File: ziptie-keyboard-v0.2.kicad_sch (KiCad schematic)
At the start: 149 parts, among them J1 Conn_01x01_Socket, J2 Conn_01x01_Socket, SW1 RotaryEncoder, U1 nice_nano

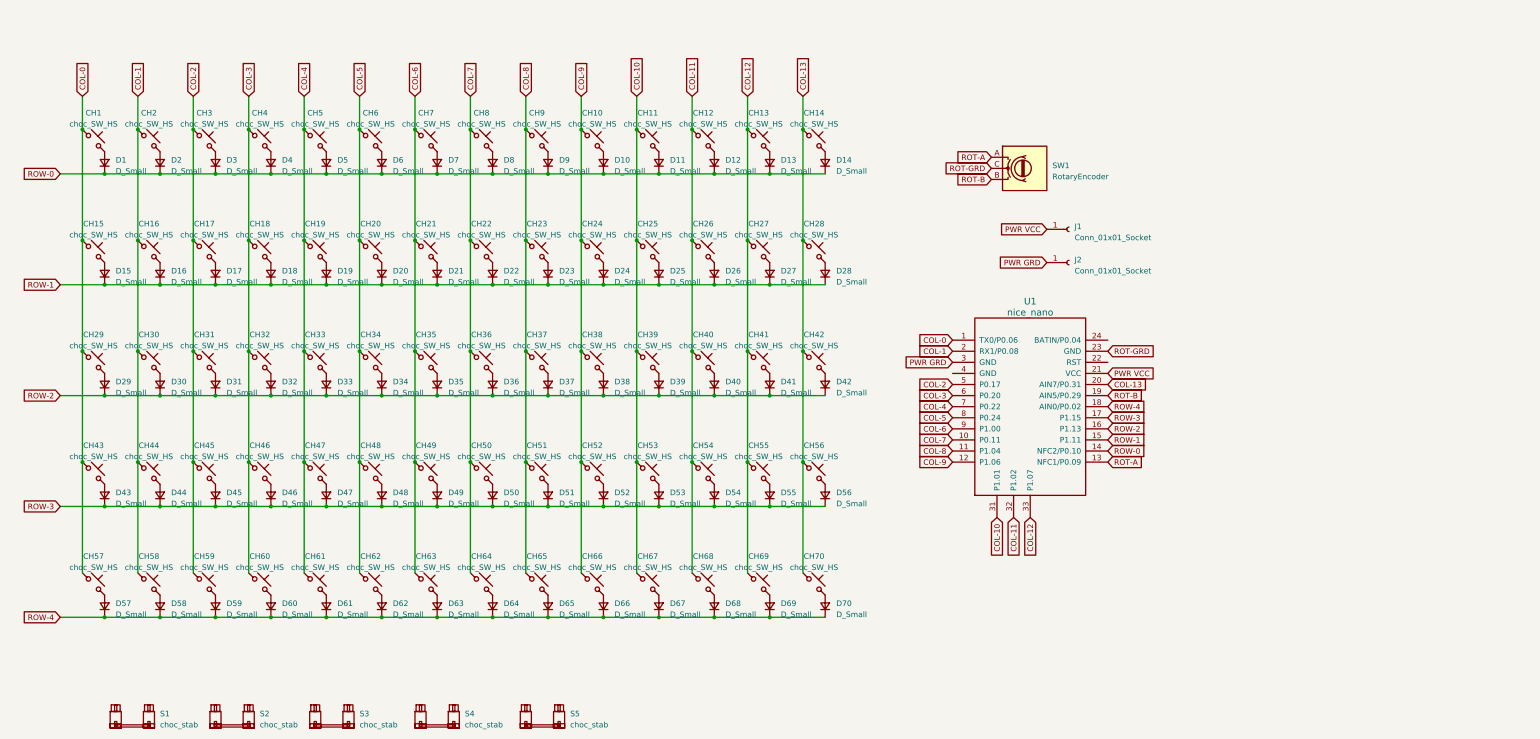
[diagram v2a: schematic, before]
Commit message: Reworked matrix, added pwr switch, btry and deco
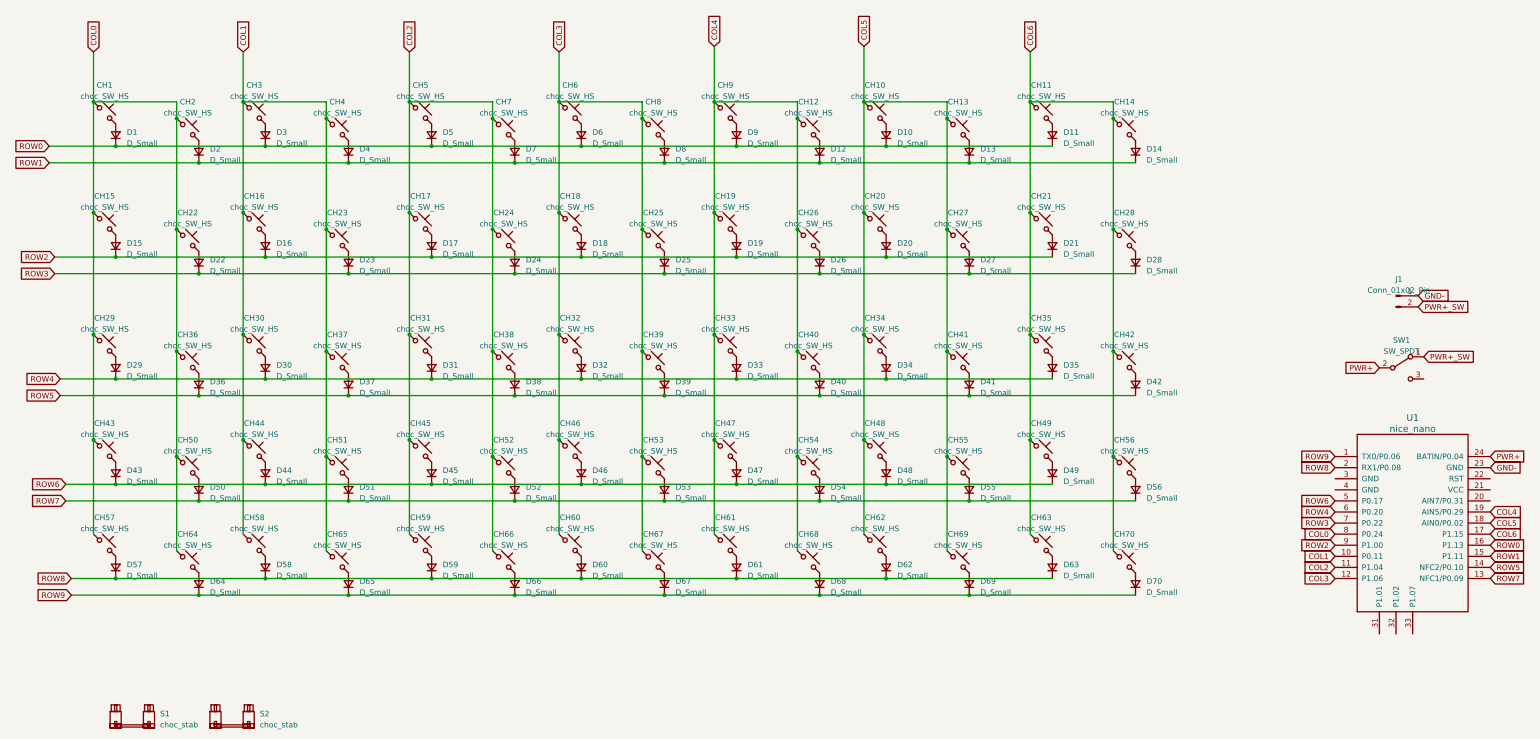
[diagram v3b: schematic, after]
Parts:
- removed CH1, CH10, CH11, CH12, CH13, CH14, CH16, CH17, CH18, CH19, CH2, CH20, CH21, CH22, CH23, CH24, CH25, CH26, CH27, CH3, CH30, CH31, CH32, CH33, CH34, CH35, CH36, CH37, CH38, CH39, CH4, CH40, CH41, CH42, CH43, CH44, CH45, CH46, CH47, CH48, CH49, CH5, CH50, CH51, CH52, CH53, CH55, CH56, CH6, CH60, CH61, CH62, CH63, CH64, CH65, CH67, CH68, CH69, CH7, CH70, CH8, CH9: choc_SW_HS, marbastlib-choc:SW_choc_v1_HS_1u, symbol marbastlib-choc:choc_SW_HS
- removed CH15, CH28: choc_SW_HS, marbastlib-choc:SW_choc_v1_HS_1.5u, symbol marbastlib-choc:choc_SW_HS
- removed CH29, CH54: choc_SW_HS, marbastlib-choc:SW_choc_v1_HS_1.75u, symbol marbastlib-choc:choc_SW_HS
- removed CH57, CH58, CH59, CH66: choc_SW_HS, marbastlib-choc:SW_choc_v1_HS_1.25u, symbol marbastlib-choc:choc_SW_HS
- removed J1, J2: Conn_01x01_Socket, Connector_Wire:SolderWire-0.1sqmm_1x01_D0.4mm_OD1mm, symbol Connector:Conn_01x01_Socket
- removed S3, S4, S5: choc_stab, marbastlib-xp-choc:STAB_choc_2u, symbol marbastlib-choc:choc_stab
- removed SW1: RotaryEncoder, Rotary_Encoder:RotaryEncoder_Alps_EC12E_Vertical_H20mm, symbol Device:RotaryEncoder
- added CH1, CH10, CH11, CH12, CH13, CH16, CH17, CH18, CH19, CH2, CH20, CH21, CH22, CH23, CH24, CH25, CH26, CH27, CH3, CH30, CH31, CH32, CH33, CH34, CH36, CH37, CH38, CH39, CH4, CH40, CH41, CH42, CH44, CH45, CH46, CH47, CH48, CH49, CH5, CH50, CH51, CH52, CH53, CH54, CH56, CH59, CH6, CH61, CH62, CH63, CH66, CH68, CH69, CH7, CH70, CH8, CH9: choc_SW_HS, PCM_Switch_Keyboard_Hotswap_Kailh:SW_Hotswap_Kailh_Choc_V1V2_Plated_1.00u, symbol PCM_marbastlib-choc:choc_SW_HS
- added CH14, CH29: choc_SW_HS, PCM_Switch_Keyboard_Hotswap_Kailh:SW_Hotswap_Kailh_Choc_V1V2_Plated_1.75u, symbol PCM_marbastlib-choc:choc_SW_HS
- added CH15, CH55, CH57, CH58, CH60, CH65, CH67: choc_SW_HS, PCM_Switch_Keyboard_Hotswap_Kailh:SW_Hotswap_Kailh_Choc_V1V2_Plated_1.50u, symbol PCM_marbastlib-choc:choc_SW_HS
- added CH28, CH64: choc_SW_HS, PCM_Switch_Keyboard_Hotswap_Kailh:SW_Hotswap_Kailh_Choc_V1V2_Plated_1.25u, symbol PCM_marbastlib-choc:choc_SW_HS
- added CH35: choc_SW_HS, PCM_Switch_Keyboard_Hotswap_Kailh:SW_Hotswap_Kailh_Choc_V1V2_Plated_2.00u, symbol PCM_marbastlib-choc:choc_SW_HS
- added CH43: choc_SW_HS, PCM_Switch_Keyboard_Hotswap_Kailh:SW_Hotswap_Kailh_Choc_V1V2_Plated_2.25u, symbol PCM_marbastlib-choc:choc_SW_HS
- added J1: Conn_01x02_Pin, Connector_JST:JST_XH_S2B-XH-A-1_1x02_P2.50mm_Horizontal, symbol Connector:Conn_01x02_Pin
- added SW1: SW_SPDT, Button_Switch_SMD:SW_SPDT_PCM12, symbol Switch:SW_SPDT
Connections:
- net at D2.2 (A): now also CH2.2
- net at D21.2 (A): now also CH21.2
- net at D44.2 (A): now also CH44.2
- net at D68.2 (A): now also CH68.2
- net at D16.2 (A): now also CH16.2
- net at D6.2 (A): now also CH6.2
- net at D23.2 (A): now also CH23.2
- net at D34.2 (A): now also CH34.2
- net at D43.2 (A): now also CH43.2
- net at D4.2 (A): now also CH4.2
- net PWR+: now reaches U1.24 (BATIN/P0.04)
- net PWR+: now also SW1.2 (B)
- net at D28.2 (A): now also CH28.2
- net at D60.2 (A): now also CH60.2
- net at D22.2 (A): now also CH22.2
- net at D24.2 (A): now also CH24.2
- net at D45.2 (A): now also CH45.2
- net at D56.2 (A): now also CH56.2
- net at D27.2 (A): now also CH27.2
- net at D63.2 (A): now also CH63.2
- net at D41.2 (A): now also CH41.2
- net at D47.2 (A): now also CH47.2
- net at D39.2 (A): now also CH39.2
- net at D67.2 (A): now also CH67.2
- net at D5.2 (A): now also CH5.2
- net at D3.2 (A): now also CH3.2
- net at D64.2 (A): now also CH64.2
- net at D70.2 (A): now also CH70.2
- net at D61.2 (A): now also CH61.2
- net at D9.2 (A): now also CH9.2
- net at D59.2 (A): now also CH59.2
- net at D19.2 (A): now also CH19.2
- net at D58.2 (A): now also CH58.2
- net at D49.2 (A): now also CH49.2
- net at D46.2 (A): now also CH46.2
- net at D52.2 (A): now also CH52.2
- net at D50.2 (A): now also CH50.2
- net at D32.2 (A): now also CH32.2
- net at D31.2 (A): now also CH31.2
- net at D51.2 (A): now also CH51.2
- net at D66.2 (A): now also CH66.2
- net at D12.2 (A): now also CH12.2
- net at D38.2 (A): now also CH38.2
- net at D18.2 (A): now also CH18.2
- net at D54.2 (A): now also CH54.2
- net at D55.2 (A): now also CH55.2
- net at D20.2 (A): now also CH20.2
- net at D1.2 (A): now also CH1.2
- net at D15.2 (A): now also CH15.2
- net at D10.2 (A): now also CH10.2
- net at D25.2 (A): now also CH25.2
- net at D65.2 (A): now also CH65.2
- net at D26.2 (A): now also CH26.2
- net at D48.2 (A): now also CH48.2
- net at D30.2 (A): now also CH30.2
- net at D13.2 (A): now also CH13.2
- net at D42.2 (A): now also CH42.2
- net at D7.2 (A): now also CH7.2
- net at D62.2 (A): now also CH62.2
- net at D57.2 (A): now also CH57.2
- net at D36.2 (A): now also CH36.2
- net at D29.2 (A): now also CH29.2
- net at D69.2 (A): now also CH69.2
- net at D8.2 (A): now also CH8.2
- net at D53.2 (A): now also CH53.2
- net at D37.2 (A): now also CH37.2
- net at D33.2 (A): now also CH33.2
- net at D17.2 (A): now also CH17.2
- net at D11.2 (A): now also CH11.2
- net at D14.2 (A): now also CH14.2
- net at D35.2 (A): now also CH35.2
- net at D40.2 (A): now also CH40.2
- net COL-0 renamed ROW9
- net ROW9: now also D64.1 (K), D65.1 (K), D66.1 (K), D67.1 (K), D68.1 (K), D69.1 (K), D70.1 (K)
- net COL-1 renamed ROW8
- net ROW8: now also D57.1 (K), D58.1 (K), D59.1 (K), D60.1 (K), D61.1 (K), D62.1 (K), D63.1 (K)
- net COL-10: no longer names the net of U1.31 (P1.01)
- net COL-11: no longer names the net of U1.32 (P1.02)
- net COL-12: no longer names the net of U1.33 (P1.07)
- net COL-13: no longer names the net of U1.20 (AIN7/P0.31)
- net COL-2 renamed ROW6
- net ROW6: now also D43.1 (K), D44.1 (K), D45.1 (K), D46.1 (K), D47.1 (K), D48.1 (K), D49.1 (K)
- net COL-3 renamed ROW4
- net ROW4: now also D29.1 (K), D30.1 (K), D31.1 (K), D32.1 (K), D33.1 (K), D34.1 (K), D35.1 (K)
- net COL-4 renamed ROW3
- net ROW3: now also D22.1 (K), D23.1 (K), D24.1 (K), D25.1 (K), D26.1 (K), D27.1 (K), D28.1 (K)
- net COL-5 renamed COL0
- net COL0: now also CH1.1, CH15.1, CH2.1, CH22.1, CH29.1, CH36.1, CH43.1, CH50.1, CH57.1, CH64.1
- net COL-6 renamed ROW2
- net ROW2: now also D15.1 (K), D16.1 (K), D17.1 (K), D18.1 (K), D19.1 (K), D20.1 (K), D21.1 (K)
- net COL-7 renamed COL1
- net COL1: now also CH16.1, CH23.1, CH3.1, CH30.1, CH37.1, CH4.1, CH44.1, CH51.1, CH58.1, CH65.1
- net COL-8 renamed COL2
- net COL2: now also CH17.1, CH24.1, CH31.1, CH38.1, CH45.1, CH5.1, CH52.1, CH59.1, CH66.1, CH7.1
- net COL-9 renamed COL3
- net COL3: now also CH18.1, CH25.1, CH32.1, CH39.1, CH46.1, CH53.1, CH6.1, CH60.1, CH67.1, CH8.1
- net PWR GRD: no longer names the net of U1.3 (GND)
- net PWR VCC: no longer names the net of U1.21 (VCC)
- net ROT-A renamed ROW7
- net ROW7: now also D50.1 (K), D51.1 (K), D52.1 (K), D53.1 (K), D54.1 (K), D55.1 (K), D56.1 (K)
- net ROT-B renamed COL4
- net COL4: now also CH12.1, CH19.1, CH26.1, CH33.1, CH40.1, CH47.1, CH54.1, CH61.1, CH68.1, CH9.1
- net ROT-GRD renamed GND-
- net GND-: now also J1.1 (Pin_1)
- removed net ROW-0: D1.1 (K), D10.1 (K), D11.1 (K), D12.1 (K), D13.1 (K), D14.1 (K), D2.1 (K), D3.1 (K), D4.1 (K), D5.1 (K), D6.1 (K), D7.1 (K), D8.1 (K), D9.1 (K), U1.14 (NFC2/P0.10)
- removed net ROW-1: D15.1 (K), D16.1 (K), D17.1 (K), D18.1 (K), D19.1 (K), D20.1 (K), D21.1 (K), D22.1 (K), D23.1 (K), D24.1 (K), D25.1 (K), D26.1 (K), D27.1 (K), D28.1 (K), U1.15 (P1.11)
- removed net ROW-2: D29.1 (K), D30.1 (K), D31.1 (K), D32.1 (K), D33.1 (K), D34.1 (K), D35.1 (K), D36.1 (K), D37.1 (K), D38.1 (K), D39.1 (K), D40.1 (K), D41.1 (K), D42.1 (K), U1.16 (P1.13)
- removed net ROW-3: D43.1 (K), D44.1 (K), D45.1 (K), D46.1 (K), D47.1 (K), D48.1 (K), D49.1 (K), D50.1 (K), D51.1 (K), D52.1 (K), D53.1 (K), D54.1 (K), D55.1 (K), D56.1 (K), U1.17 (P1.15)
- removed net ROW-4: D57.1 (K), D58.1 (K), D59.1 (K), D60.1 (K), D61.1 (K), D62.1 (K), D63.1 (K), D64.1 (K), D65.1 (K), D66.1 (K), D67.1 (K), D68.1 (K), D69.1 (K), D70.1 (K), U1.18 (AIN0/P0.02)
- new net COL5: CH10.1, CH13.1, CH20.1, CH27.1, CH34.1, CH41.1, CH48.1, CH55.1, CH62.1, CH69.1, U1.18 (AIN0/P0.02)
- new net COL6: CH11.1, CH14.1, CH21.1, CH28.1, CH35.1, CH42.1, CH49.1, CH56.1, CH63.1, CH70.1, U1.17 (P1.15)
- new net PWR+_SW: J1.2 (Pin_2), SW1.1 (A)
- new net ROW0: D1.1 (K), D10.1 (K), D11.1 (K), D3.1 (K), D5.1 (K), D6.1 (K), D9.1 (K), U1.16 (P1.13)
- new net ROW1: D12.1 (K), D13.1 (K), D14.1 (K), D2.1 (K), D4.1 (K), D7.1 (K), D8.1 (K), U1.15 (P1.11)
- new net ROW5: D36.1 (K), D37.1 (K), D38.1 (K), D39.1 (K), D40.1 (K), D41.1 (K), D42.1 (K), U1.14 (NFC2/P0.10)
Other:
- moved on the sheet: U1
